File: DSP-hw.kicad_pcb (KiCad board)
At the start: 4 copper layers, 184 x 65.6 mm, 107 parts, among them J1 NC3MAH, J10 AudioJack3, J11 AudioJack3, J2 NC3MAH, J3 NC3MAH, J4 NC3MAH, J5 XLR3_AudioJack3_Combo_Ground, J6 XLR3_AudioJack3_Combo_Ground, J7 USB_C_Receptacle_USB2.0_16P, J8 Conn_01x04_Pin, J9 Conn_01x06_Pin, Q1 BC327, Q2 AO3400A, SW1 SW_Push, SW2 SW_Push, SW6 SW_SPST, SW7 SW_SPST, SW8 SW_Push, U1 ADAU1701, U2 CAT24C256, U3 AMS1117-3.3, U4 STM32F411RETx, U5 TME-0505S, U6 ADUM3160, Y1 12.228M

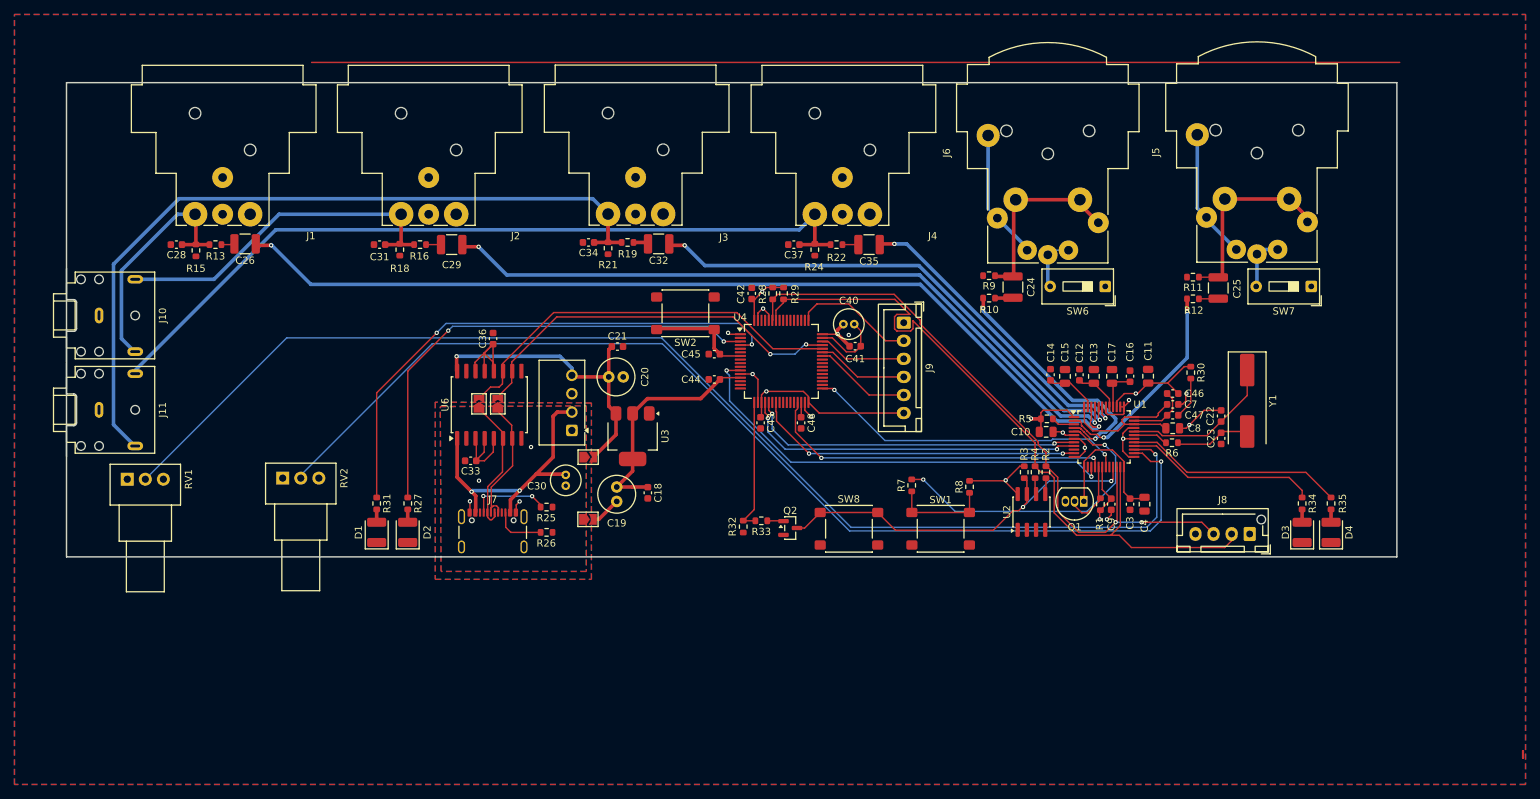
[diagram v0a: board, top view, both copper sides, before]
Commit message: cambiato connettori jack
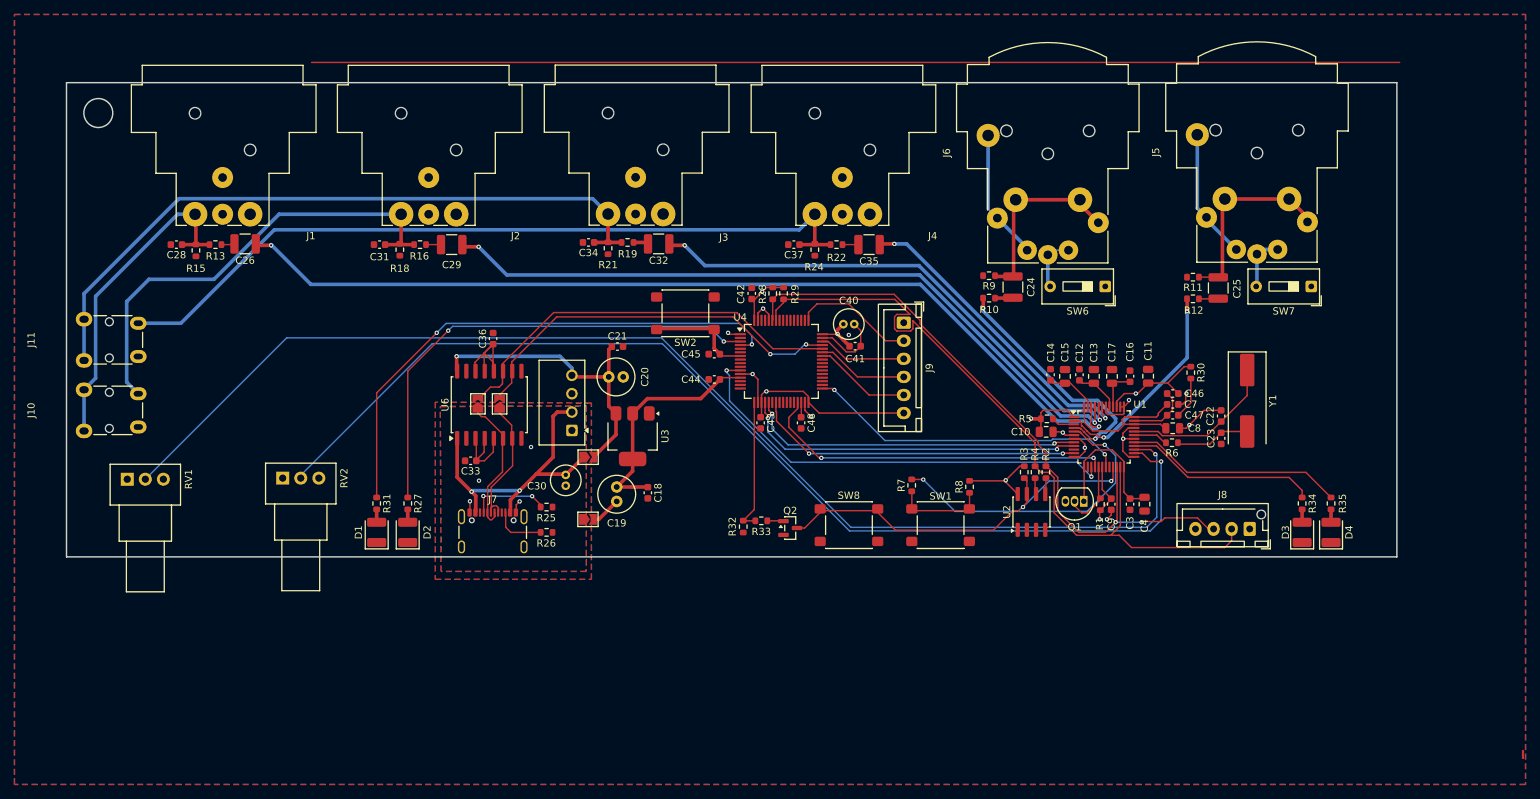
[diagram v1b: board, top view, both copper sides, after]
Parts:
- J10, J11: footprint Connector_Audio:Jack_3.5mm_CUI_SJ1-3523N_Horizontal -> Connector_Audio:Jack_3.5mm_Lumberg_1503_07_Horizontal
- moved J10 16.1 mm to (60.5, 77.0), turned to 90 degrees
- moved J11 7.13 mm to (60.5, 67.2), turned to 90 degrees
- moved J8 0.70 mm to (221.8, 90.5)
- moved SW1 0.50 mm to (179.0, 90.0)
- moved SW8 0.50 mm to (166.3, 90.0)
- moved JP3 0.25 mm to (118.0, 73.2)
- moved JP2 0.15 mm to (115.0, 73.2)
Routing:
- net Net-(C31-Pad1): track 48.8 -> 64.5 mm
- net Net-(C28-Pad1): track 33.4 -> 45.8 mm
- net Net-(C34-Pad1): track 107.0 -> 95.7 mm
- net Net-(C37-Pad1): track 111.8 -> 108.2 mm
- net +5VA: track 41.0 -> 44.4 mm
- net /LRCK_2: track 48.3 -> 49.2 mm
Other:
- outline, holes or cut-outs redrawn

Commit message: passato tutto a due layer
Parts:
- moved RV1 6.50 mm to (73.0, 83.7)
- moved RV2 1.91 mm to (89.9, 83.3)
- moved C42 0.36 mm to (153.2, 58.1)
- moved C10 0.10 mm to (193.6, 77.0)
- moved R5 0.10 mm to (193.7, 75.2)
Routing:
- net +3V3: track 111.1 -> 453.6 mm, vias 8 -> 9
- net GND: track 64.8 -> 83.0 mm, vias 11 -> 18
- net Net-(U6-PIN): track 15.8 -> 12.1 mm
- net /MP8: track 171.4 -> 168.3 mm
- net /WP: track 54.7 -> 53.5 mm
- net /MP9: track 150.6 -> 149.7 mm
- removed copper zone on In1.Cu, net +3V3
- removed copper zone on In2.Cu, net +3V3
- removed copper zone on In1.Cu, net GND
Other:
- board size 184 x 65.6 mm -> 182 x 64.6 mm
- copper layers 4 -> 2

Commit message: aggiunto oscillatore allo schematico
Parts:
- added C27: 100n, Capacitor_SMD:C_0603_1608Metric, F.Cu at (196.0, 73.0)
- added C49: 100n, Capacitor_SMD:C_0603_1608Metric, F.Cu at (148.5, 63.0)
- added C50: 100n, Capacitor_SMD:C_0603_1608Metric, F.Cu at (162.5, 75.5)
- C17: value 10u -> 47u; footprint Capacitor_SMD:C_0805_2012Metric -> Capacitor_THT:C_Radial_D5.0mm_H11.0mm_P2.00mm
- C7: value 1u -> 100n
- moved R27 40.5 mm to (145.8, 86.5)
- moved D1 40.5 mm to (141.5, 90.5)
- moved R31 40.5 mm to (141.5, 86.5)
- moved D2 40.5 mm to (145.8, 90.5)
- moved SW2 5.98 mm to (142.2, 66.5), turned to -90 degrees
- moved RV2 3.60 mm to (93.5, 83.5)
- moved C17 3.44 mm to (203.0, 66.0), turned to 0 degrees
- moved C16 1.80 mm to (203.5, 70.0), turned to 0 degrees
- moved C36 1.70 mm to (116.0, 65.5)
- moved J9 0.90 mm to (173.0, 62.0)
- moved J10 0.88 mm to (60.5, 77.8)
- moved C42 0.70 mm to (152.5, 58.1)
- moved J11 0.38 mm to (60.5, 66.8)
- moved C45 0.16 mm to (147.7, 66.5)
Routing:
- net +3V3: track 453.6 -> 395.9 mm
- net Net-(U4-PC15): track 73.7 -> 26.7 mm
- net Net-(U4-PC14): track 66.9 -> 24.8 mm
- net GND: track 83.0 -> 94.1 mm, vias 18 -> 27
- net /SCL: track 102.6 -> 95.6 mm
- net Net-(U1-~{RESET}): track 42.6 -> 46.3 mm
- net Net-(U6-PIN): track 12.1 -> 8.40 mm
- net Net-(U1-PVDD): track 22.5 -> 24.8 mm
- net /MP9: track 149.7 -> 147.5 mm
- net Net-(U4-NRST): track 14.8 -> 16.9 mm
- net Net-(U1-CM): track 5.91 -> 7.70 mm
- net Net-(C37-Pad1): track 108.2 -> 109.7 mm
- net Net-(C31-Pad1): track 64.5 -> 65.7 mm
- net /DOUT: track 62.2 -> 63.2 mm
- net Net-(C28-Pad1): track 45.8 -> 46.6 mm
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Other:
- board size 182 x 64.6 mm -> 183.7 x 64.6 mm

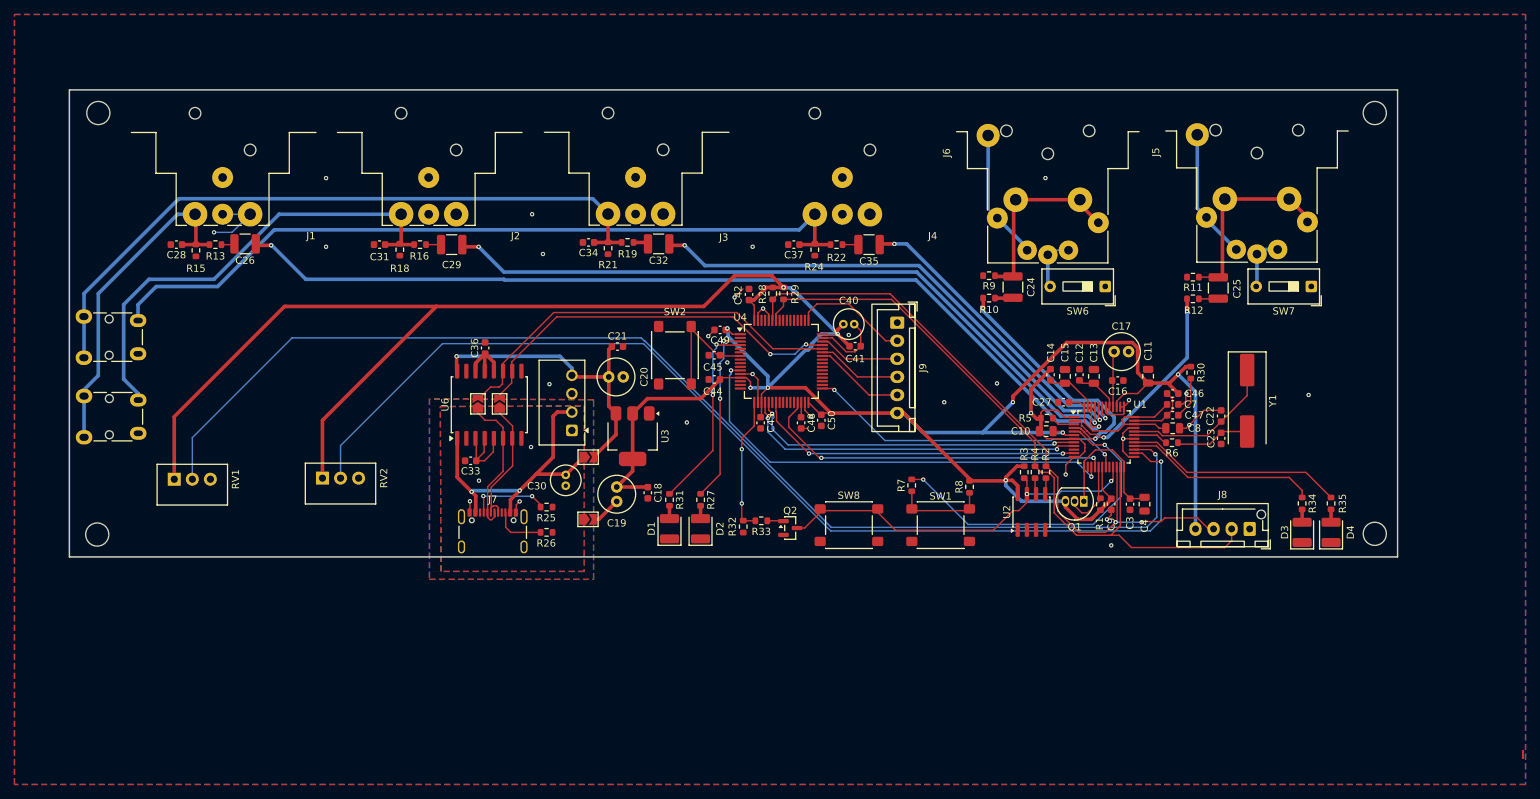
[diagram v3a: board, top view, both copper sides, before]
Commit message: sostituito dei componenti non piu disponibili
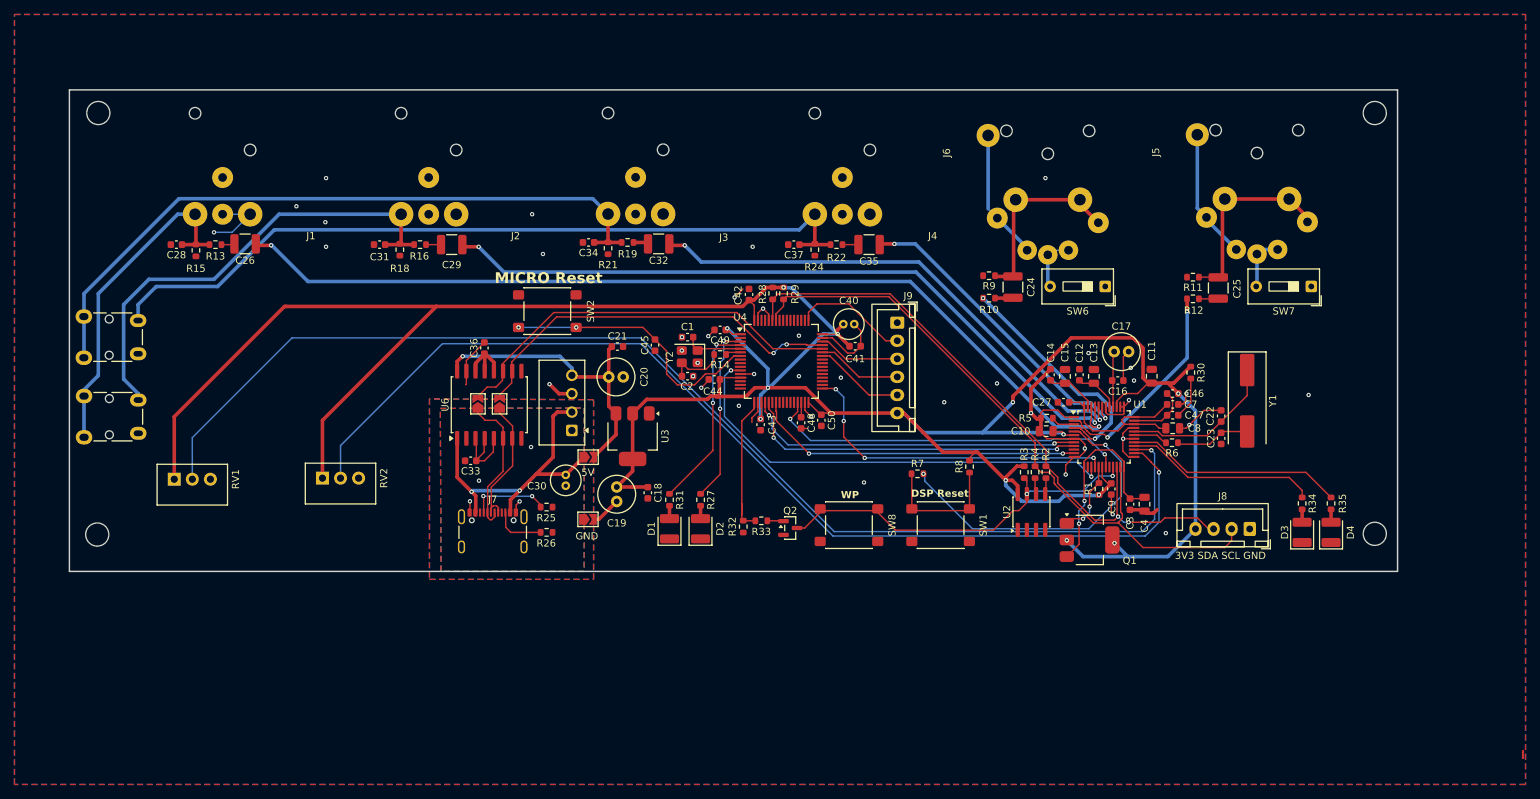
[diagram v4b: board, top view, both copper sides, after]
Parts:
- added C1: 12p, Capacitor_SMD:C_0603_1608Metric, F.Cu at (144.0, 64.0)
- added C2: 12p, Capacitor_SMD:C_0603_1608Metric, F.Cu at (144.0, 69.4)
- added R14: 0, Resistor_SMD:R_0603_1608Metric, F.Cu at (148.5, 66.4)
- added Y2: Crystal_GND24, Crystal:Crystal_SMD_3225-4Pin_3.2x2.5mm, F.Cu at (144.3, 66.7)
- J8: footprint Connector_JST:JST_XH_B4B-XH-AM_1x04_P2.50mm_Vertical -> Connector_JST:JST_XH_B4B-XH-A_1x04_P2.50mm_Vertical
- Q1: footprint Package_TO_SOT_THT:TO-92_Inline -> Package_TO_SOT_SMD:SOT-223-3_TabPin2
- moved SW2 18.7 mm to (124.6, 60.4), turned to 180 degrees
- moved C45 8.32 mm to (139.5, 65.1), turned to -90 degrees
- moved Q1 5.41 mm to (199.6, 92.0), turned to 0 degrees
- moved R8 2.80 mm to (183.0, 81.9)
- moved R1 2.11 mm to (200.9, 85.0)
- moved C9 2.11 mm to (202.6, 85.0)
- moved R7 1.79 mm to (175.8, 82.9), turned to 0 degrees
- moved C11 0.50 mm to (208.2, 69.4)
- moved C43 0.25 mm to (154.1, 76.1)
- moved C36 0.10 mm to (115.9, 65.5)
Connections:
- U4 pad 20: /BCLK_1 -> /LRCK_1
- U4 pad 21: /LRCK_1 -> /BCLK_1
- U4 pad 29: /LRCK_2 -> /BCLK_2
- U4 pad 33: /BCLK_2 -> /LRCK_2
- U4 pad 5: unconnected-(U4-PH0-Pad5) -> Net-(U4-PH0)
- U4 pad 6: unconnected-(U4-PH1-Pad6) -> Net-(U4-PH1)
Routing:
- net GND: track 94.1 -> 115.1 mm, vias 27 -> 40
- net Net-(U4-NRST): track 16.9 -> 37.5 mm, vias 0 -> 2
- net +3V3: track 395.9 -> 416.2 mm, vias 9 -> 12
- net Net-(Q1-C): track 19.9 -> 28.6 mm, vias 0 -> 2
- net Net-(C2-Pad2): track 0.00 -> 8.30 mm
- net Net-(U4-PH0): track 0.00 -> 8.11 mm
- net /BCLK_2: track 44.8 -> 50.4 mm
- net Net-(R7-Pad1): track 13.5 -> 18.4 mm
- net /SCL: track 95.6 -> 91.6 mm
- net /SDA: track 91.9 -> 88.0 mm
- net /LRCK_2: track 49.2 -> 46.0 mm, vias 2 -> 4
- net Net-(U4-PH1): track 0.00 -> 1.87 mm
- net /WP_M: track 18.8 -> 20.4 mm, vias 2 -> 0
- net /ADC1: track 34.0 -> 32.8 mm
- net /Micro/UART1_TX: track 12.7 -> 11.8 mm
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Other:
- board size 183.7 x 64.6 mm -> 183.7 x 66.6 mm
- board text added: "3V3 SDA SCL GND"
- board text added: "5V"
- board text added: "DSP Reset"
- board text added: "GND"
- board text added: "MICRO Reset"
- board text added: "WP"

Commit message: modifiche suggerite da osti
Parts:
- added H1: MountingHole, MountingHole:MountingHole_3.2mm_M3_Pad_Via, F.Cu at (63.0, 35.0)
- added H2: MountingHole, MountingHole:MountingHole_3.2mm_M3_Pad_Via, F.Cu at (239.0, 35.0)
- added H3: MountingHole, MountingHole:MountingHole_3.2mm_M3_Pad_Via, F.Cu at (239.0, 92.0)
- added H4: MountingHole, MountingHole:MountingHole_3.2mm_M3_Pad_Via, F.Cu at (63.0, 92.0)
- C22, C23: value 22p -> 18p
- R6: value 100 -> 80
- Y1: footprint Crystal:Crystal_SMD_HC49-SD -> Crystal:Crystal_SMD_3225-4Pin_3.2x2.5mm
- moved Y1 7.04 mm to (216.4, 77.8), turned to 180 degrees
- moved RV2 4.53 mm to (93.0, 88.0)
- moved RV1 4.35 mm to (73.0, 88.0)
- moved C23 2.93 mm to (216.6, 80.7), turned to 180 degrees
- moved R26 2.40 mm to (124.5, 93.4)
- moved J7 1.97 mm to (117.2, 93.9)
- moved C22 1.35 mm to (216.5, 75.2), turned to 0 degrees
- moved C1 0.60 mm to (144.6, 64.0)
- moved J8 0.10 mm to (221.8, 90.4)
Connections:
- Y1 pad 2: Net-(C23-Pad2) -> GND
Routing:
- net +3V3: track 416.2 -> 473.9 mm, vias 12 -> 11
- net GND: track 115.1 -> 126.4 mm, vias 40 -> 204
- net Net-(U1-MCLKI): track 21.7 -> 14.9 mm
- net Net-(U4-NRST): track 37.5 -> 43.7 mm
- net /MP9: track 147.0 -> 152.2 mm
- net /MP8: track 168.5 -> 173.6 mm
- net Net-(C23-Pad2): track 10.3 -> 5.72 mm
- net +5VA: track 44.4 -> 48.8 mm
- net GNDA: track 3.19 -> 7.21 mm
- net /Micro/D-: track 20.1 -> 22.6 mm
- net /Micro/D+: track 19.2 -> 21.6 mm
- net Net-(J7-CC1): track 11.1 -> 13.1 mm
- net Net-(U4-PH1): track 1.87 -> 2.51 mm
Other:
- board size 183.7 x 66.6 mm -> 185 x 66.6 mm
